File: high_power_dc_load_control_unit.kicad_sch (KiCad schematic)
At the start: 53 parts, among them IC1 STPS60L45CW, IC3 LT8711EFE#TRPBF, J4 XT60-M, J5 XT60-M, Q1 RS6P100BHTB1, Q2 PMOS, Q4 NMOS, U1 UCC5350MCD, U2 LTC3525ESC6-5-TRMPBF

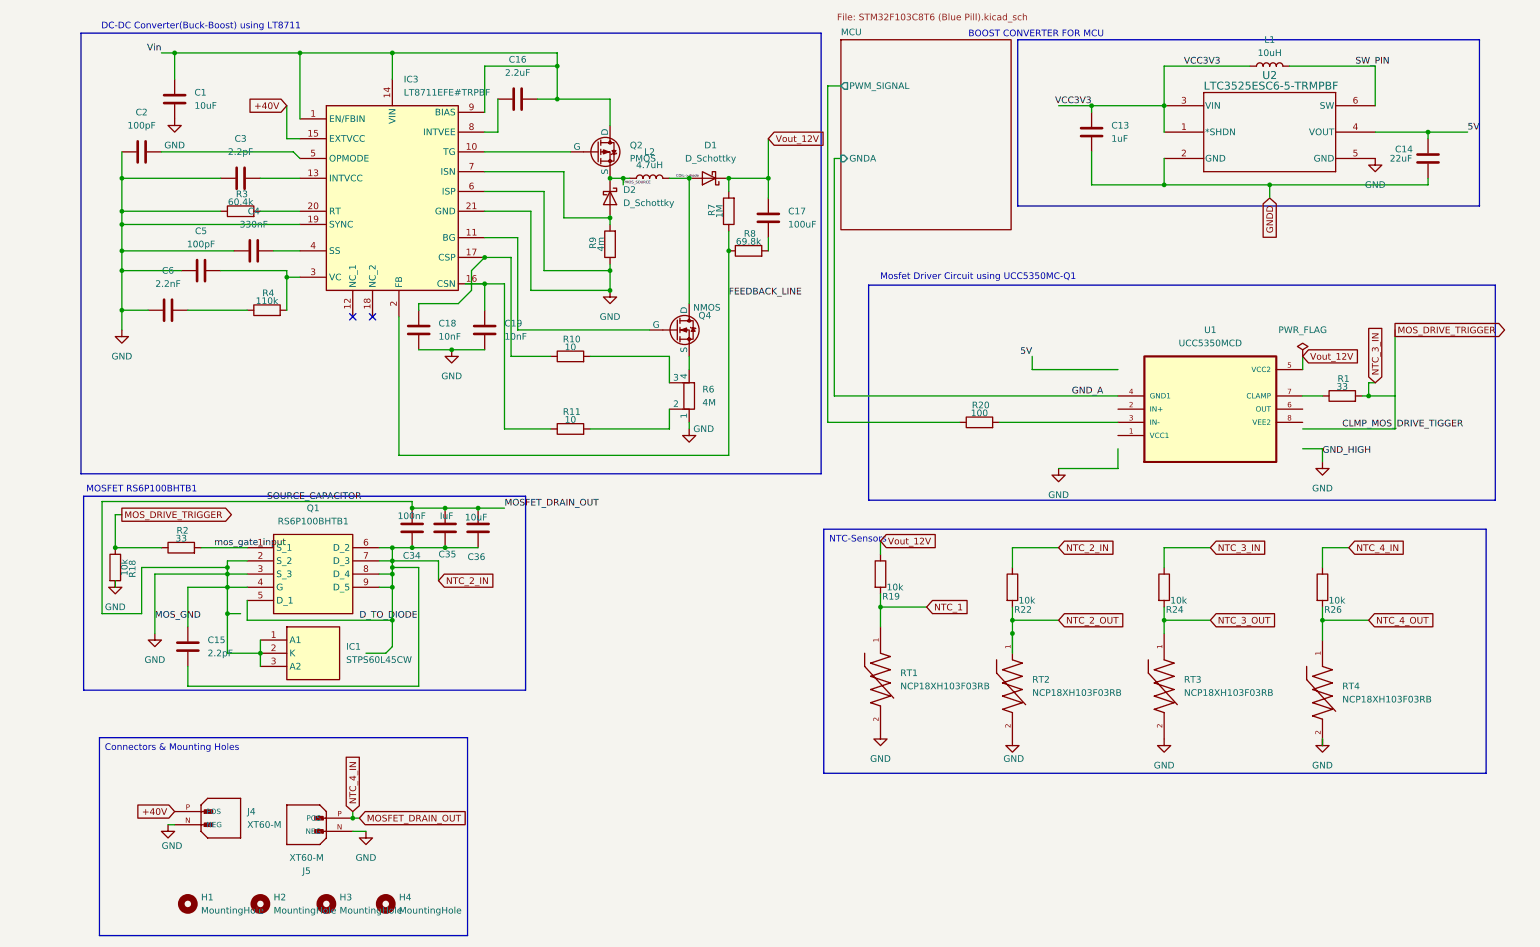
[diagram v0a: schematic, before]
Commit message: Added .gitignore to prevent ZIP files from being tracked
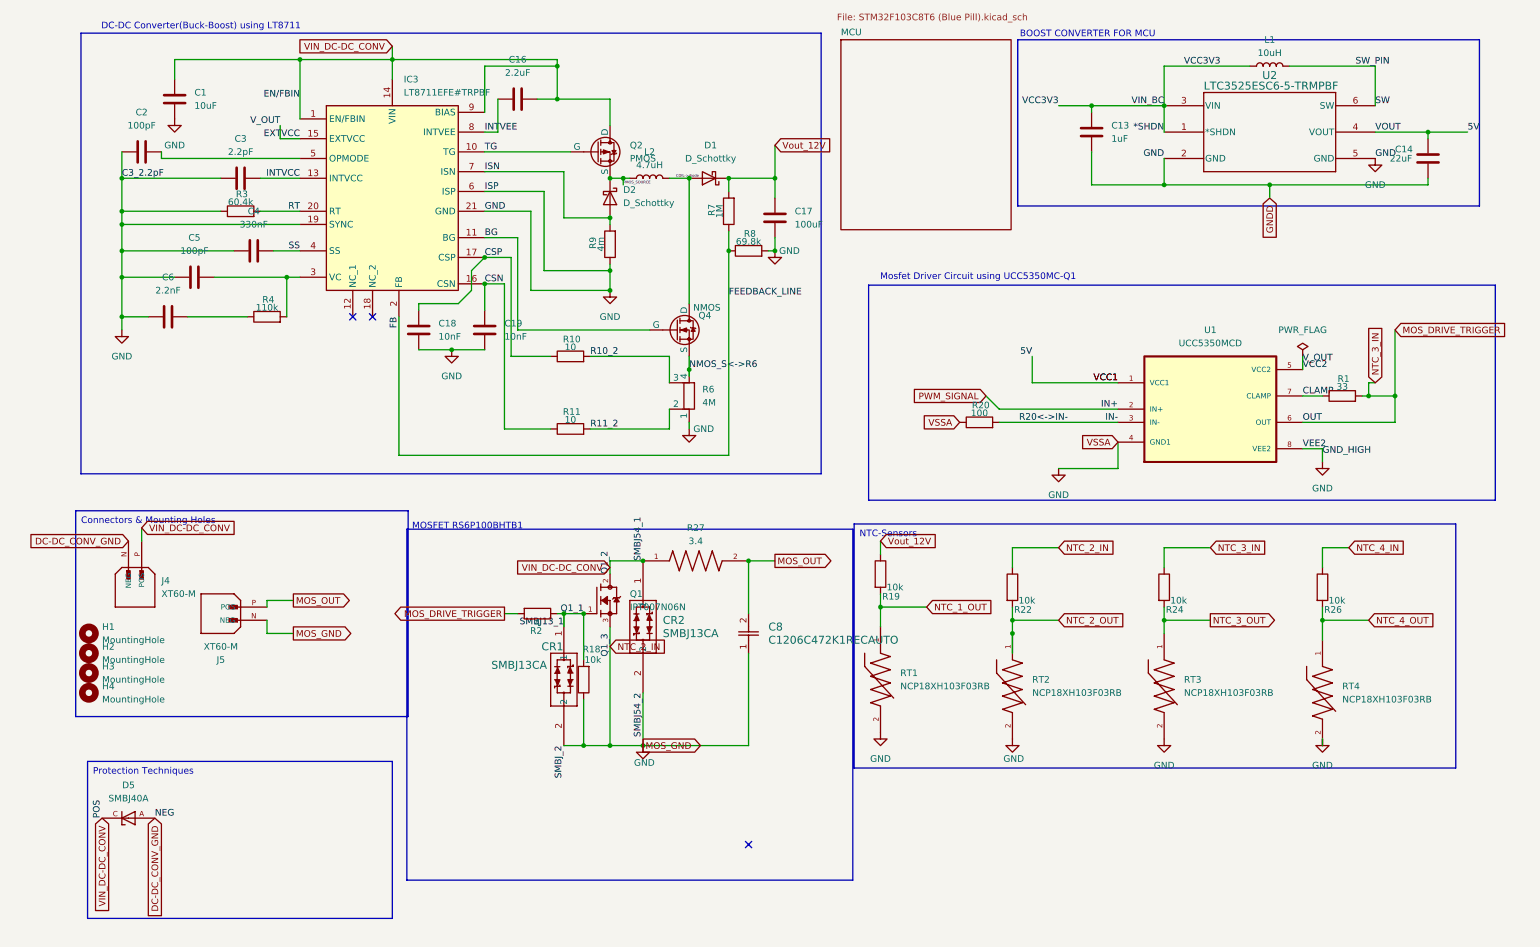
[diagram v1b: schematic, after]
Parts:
- removed C15: 2.2pF, Capacitor_SMD:C_0603_1608Metric, symbol Device:C
- removed C34: 100nF, Capacitor_SMD:C_0603_1608Metric, symbol Device:C
- removed C35: IuF, Capacitor_SMD:C_0603_1608Metric, symbol Device:C
- removed C36: 10uF, Capacitor_SMD:C_0603_1608Metric, symbol Device:C
- removed IC1: STPS60L45CW, TO545P515X1560X2445-3P, symbol STPS60L45CW:STPS60L45CW
- removed Q1: RS6P100BHTB1, RS6G120BGTB1, symbol RS6P100BHTB1:RS6P100BHTB1
- added C8: C1206C472K1RECAUTO, SNUBBER_CAPACITOR:CAPC340180_88N_KEM-L, symbol 2025-04-01_14-25-35:C1206C472K1RECAUTO
- added CR1, CR2: SMBJ13CA, SMBJ13CA:DO214AC_LTF-L, symbol 2025-04-01_14-40-45:SMBJ13CA
- added D5: SMBJ40A, SMBJ40A:DIOM4336X265N, symbol SMBJ40A:SMBJ40A
- added Q1: IPT007N06N, Package_TO_SOT_SMD:TO-263-7_TabPin8, symbol IRFP4468PBF:IRFP4468PBF
- added R27: 3.4, SNUBBER_RES:RESC6331X70N, symbol CRCW25123R30JNEG:CRCW25123R30JNEG
- IC3: footprint SOP65P640X120-21N -> AP7343-30W5-7:SOP65P640X120-21N
- J4, J5: footprint XT60-M:AMASS_XT60-M -> Connector_AMASS:AMASS_XT60PW-M_1x02_P7.20mm_Horizontal
- R2: value 33 -> 4
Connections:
- net GNDD is gone; now on net GND: C13.1, C14.1, U2.2 (GND)
- net GND_A is gone; now on net GND: U1.4 (GND1)
- net MCU/PWM_SIGNAL is gone; now on net GND: R20.1
- net NTC_2_IN is gone; now on net GND: R22.1
- net NTC_3_IN is gone; now on net MOS_DRIVE_TRIGGER: R1.2, R24.1
- net mos_gate_input is gone; now on net MOS_DRIVE_TRIGGER: R2.2
- net 5V: now also U1.1 (VCC1)
- net GND: now also C17.2, R18.1, R8.2, U1.8 (VEE2), C8.1, CR1.2, CR2.2, Q1.3; no longer J4.N (NEG), J5.P (POS), R18.2, R26.1
- net MOS_DRIVE_TRIGGER: now also U1.6 (OUT); no longer R18.1, R2.1
- net Vout_12V: no longer U1.5 (VCC2)
- net ISN: now reaches D2.2 (A), IC3.7 (ISN), R9.2
- net CSN: now reaches C19.2, IC3.16 (CSN), R11.1
- net R11_2: now reaches R11.2, R6.2
- net PWM_SIGNAL: now reaches U1.2 (IN+)
- net IN-: now reaches R20.2, U1.3 (IN-)
- net CLAMP: now reaches R1.1, U1.7 (CLAMP)
- net INTVEE: now reaches C16.1, IC3.8 (INTVEE)
- net INTVCC: now reaches C3.2, IC3.13 (INTVCC)
- net TG: now reaches IC3.10 (TG), Q2.2 (G)
- net BG: now reaches IC3.11 (BG), Q4.2 (G)
- net CSP: now reaches C18.2, IC3.17 (CSP), R10.1
- net RT: now reaches IC3.20 (RT), R3.2
- net SS: now reaches C4.2, IC3.4 (SS)
- net R10_2: now reaches R10.2, R6.3
- net NMOS_S<->R6: now reaches Q4.3 (S), R6.4
- net +40V renamed EXTVCC
- net EXTVCC: now also U1.5 (VCC2); no longer J4.P (POS)
- net FEEDBACK_LINE renamed FB
- net NTC_1 renamed NTC_1_OUT
- net SW_PIN renamed SW
- net VCC3V3 renamed *SHDN
- net Vin renamed VIN_DC-DC_CONV
- net VIN_DC-DC_CONV: now also J4.P (POS), CR2.1, D5.C, Q1.2, R27.1
- new net DC-DC_CONV_GND: D5.A, J4.N (NEG)
- new net MOS_OUT: C8.2, J5.P (POS), R27.2
- new net NTC_4_IN: R26.1
- new net Q1_1: CR1.1, Q1.1, R18.2, R2.1
- no-connect marks 2 -> 3
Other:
- sheet MCU ports: added none; removed GNDA, PWM_SIGNAL
- moved on the sheet: C17, C5, C6, H1, H2, H3, H4, J4, J5, R4
